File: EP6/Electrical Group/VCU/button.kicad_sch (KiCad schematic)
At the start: 5 parts

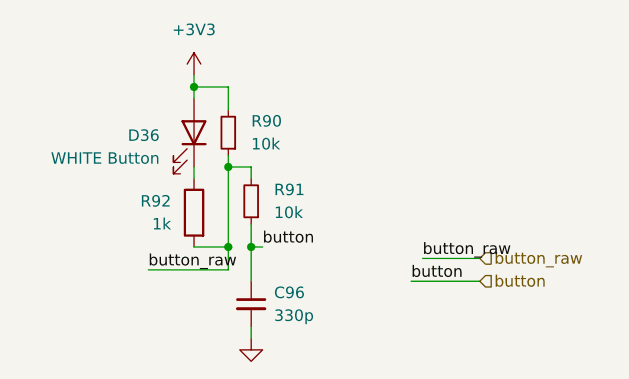
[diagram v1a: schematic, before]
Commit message: replace MCU with STM32H7431
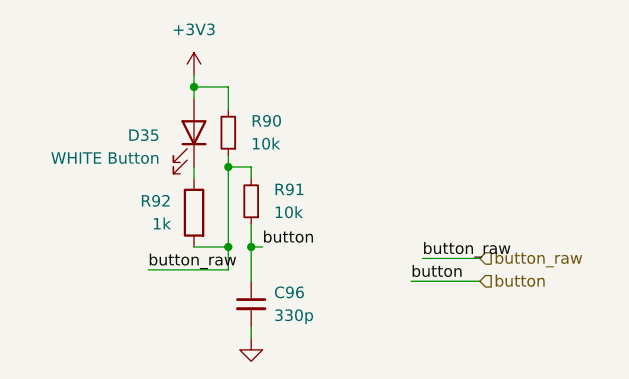
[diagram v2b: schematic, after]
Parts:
- renumbered D36 to D35
